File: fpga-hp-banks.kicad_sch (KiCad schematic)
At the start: 9 parts, among them U34 XCAU25P-2FFVB676I

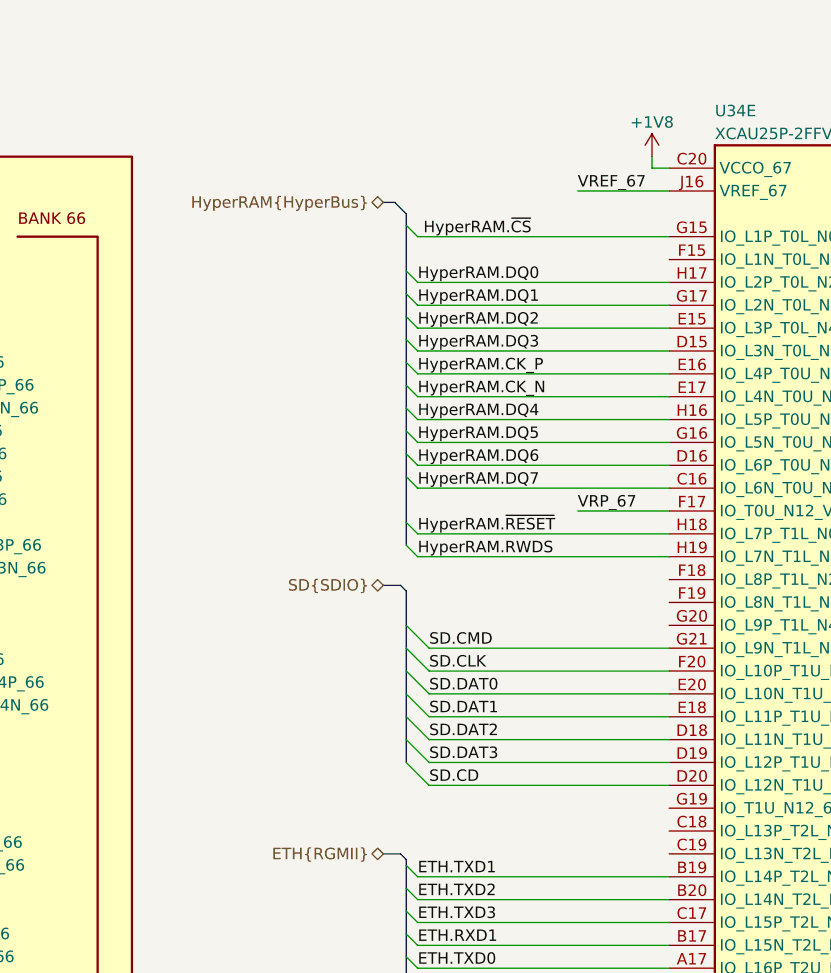
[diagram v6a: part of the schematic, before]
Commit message: [#67016] Add HyperRam layout
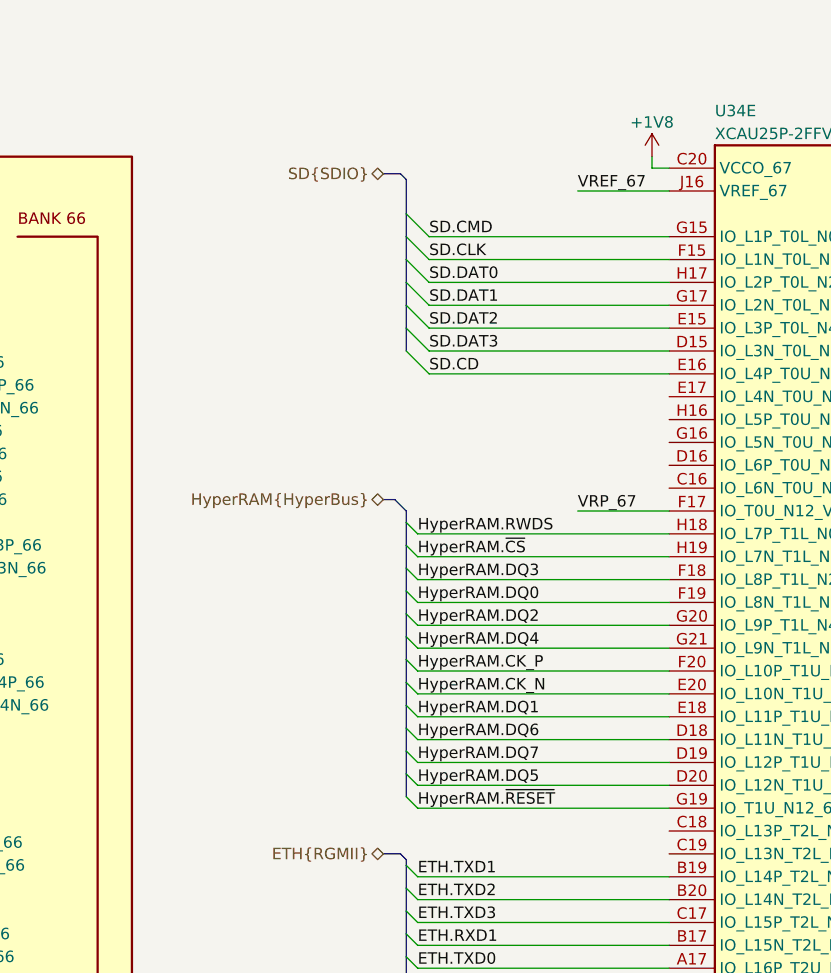
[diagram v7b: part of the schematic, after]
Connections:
- net HyperRAM.CK_N: now also U34.E20 (IO_L10N_T1U_N7_QBC_AD4N_67); no longer U34.E17 (IO_L4N_T0U_N7_DBC_AD7N_67)
- net HyperRAM.CK_P: now also U34.F20 (IO_L10P_T1U_N6_QBC_AD4P_67); no longer U34.E16 (IO_L4P_T0U_N6_DBC_AD7P_67)
- net HyperRAM.DQ0: now also U34.F19 (IO_L8N_T1L_N3_AD5N_67); no longer U34.H17 (IO_L2P_T0L_N2_67)
- net HyperRAM.DQ1: now also U34.E18 (IO_L11P_T1U_N8_GC_67); no longer U34.G17 (IO_L2N_T0L_N3_67)
- net HyperRAM.DQ2: now also U34.G20 (IO_L9P_T1L_N4_AD12P_67); no longer U34.E15 (IO_L3P_T0L_N4_AD15P_67)
- net HyperRAM.DQ3: now also U34.F18 (IO_L8P_T1L_N2_AD5P_67); no longer U34.D15 (IO_L3N_T0L_N5_AD15N_67)
- net HyperRAM.DQ4: now also U34.G21 (IO_L9N_T1L_N5_AD12N_67); no longer U34.H16 (IO_L5P_T0U_N8_AD14P_67)
- net HyperRAM.DQ5: now also U34.D20 (IO_L12N_T1U_N11_GC_67); no longer U34.G16 (IO_L5N_T0U_N9_AD14N_67)
- net HyperRAM.DQ6: now also U34.D18 (IO_L11N_T1U_N9_GC_67); no longer U34.D16 (IO_L6P_T0U_N10_AD6P_67)
- net HyperRAM.DQ7: now also U34.D19 (IO_L12P_T1U_N10_GC_67); no longer U34.C16 (IO_L6N_T0U_N11_AD6N_67)
- net HyperRAM.RWDS: now also U34.H18 (IO_L7P_T1L_N0_QBC_AD13P_67); no longer U34.H19 (IO_L7N_T1L_N1_QBC_AD13N_67)
- net HyperRAM.~{CS}: now also U34.H19 (IO_L7N_T1L_N1_QBC_AD13N_67); no longer U34.G15 (IO_L1P_T0L_N0_DBC_67)
- net HyperRAM.~{RESET}: now also U34.G19 (IO_T1U_N12_67); no longer U34.H18 (IO_L7P_T1L_N0_QBC_AD13P_67)
- net SD.CD: now also U34.E16 (IO_L4P_T0U_N6_DBC_AD7P_67); no longer U34.D20 (IO_L12N_T1U_N11_GC_67)
- net SD.CLK: now also U34.F15 (IO_L1N_T0L_N1_DBC_67); no longer U34.F20 (IO_L10P_T1U_N6_QBC_AD4P_67)
- net SD.CMD: now also U34.G15 (IO_L1P_T0L_N0_DBC_67); no longer U34.G21 (IO_L9N_T1L_N5_AD12N_67)
- net SD.DAT0: now also U34.H17 (IO_L2P_T0L_N2_67); no longer U34.E20 (IO_L10N_T1U_N7_QBC_AD4N_67)
- net SD.DAT1: now also U34.G17 (IO_L2N_T0L_N3_67); no longer U34.E18 (IO_L11P_T1U_N8_GC_67)
- net SD.DAT2: now also U34.E15 (IO_L3P_T0L_N4_AD15P_67); no longer U34.D18 (IO_L11N_T1U_N9_GC_67)
- net SD.DAT3: now also U34.D15 (IO_L3N_T0L_N5_AD15N_67); no longer U34.D19 (IO_L12P_T1U_N10_GC_67)

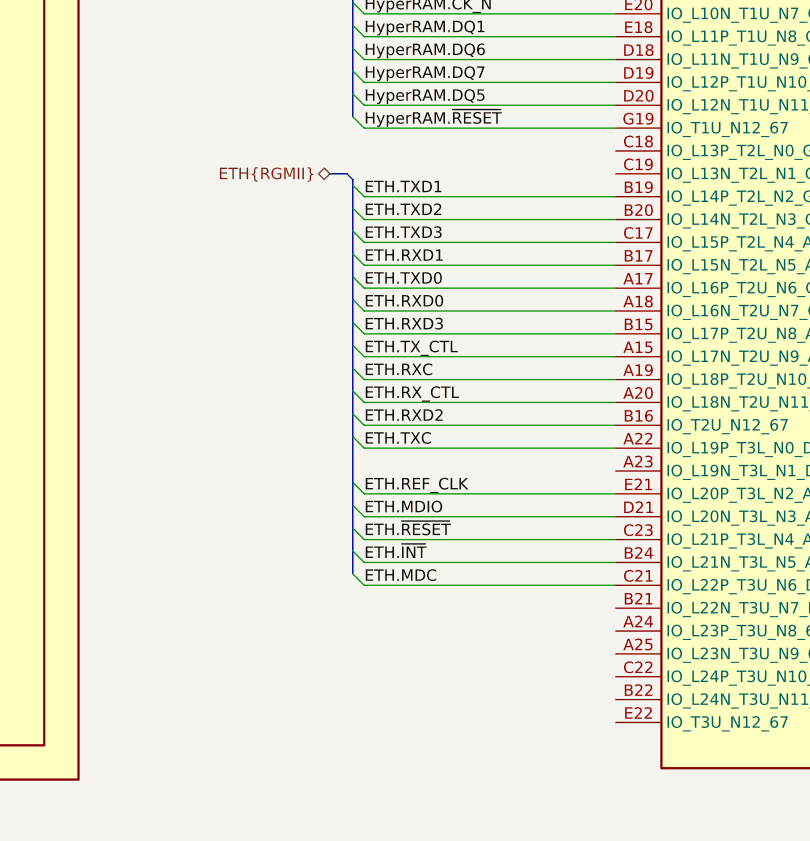
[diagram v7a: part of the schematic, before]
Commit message: [#67016] Remap RGMII interface
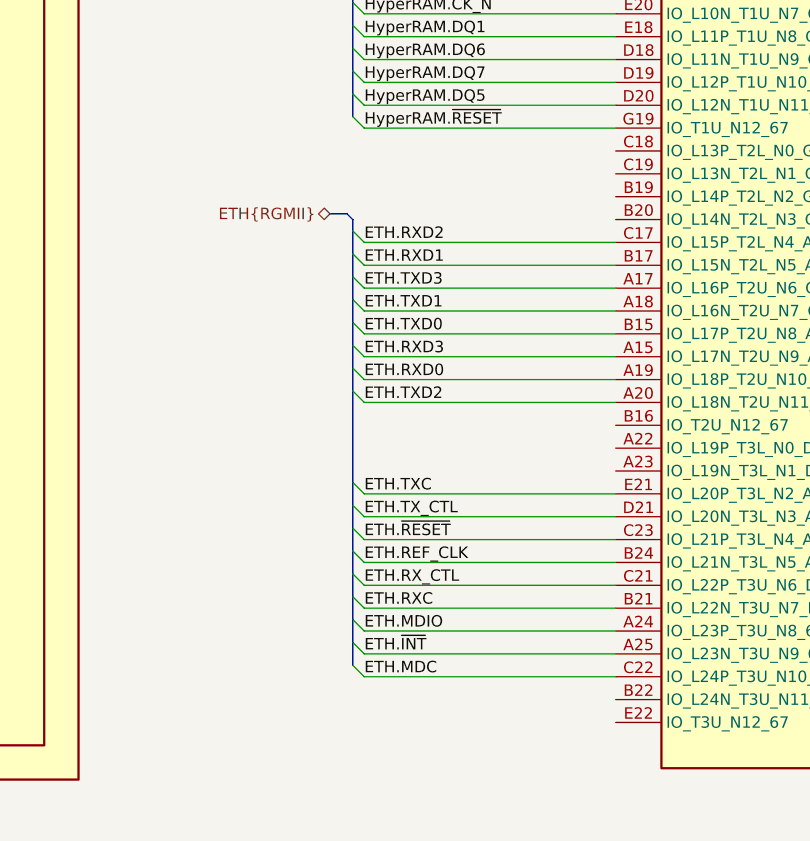
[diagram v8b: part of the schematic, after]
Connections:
- net ETH.MDC: now also U34.C22 (IO_L24P_T3U_N10_67); no longer U34.C21 (IO_L22P_T3U_N6_DBC_AD0P_67)
- net ETH.MDIO: now also U34.A24 (IO_L23P_T3U_N8_67); no longer U34.D21 (IO_L20N_T3L_N3_AD1N_67)
- net ETH.REF_CLK: now also U34.B24 (IO_L21N_T3L_N5_AD8N_67); no longer U34.E21 (IO_L20P_T3L_N2_AD1P_67)
- net ETH.RXC: now also U34.B21 (IO_L22N_T3U_N7_DBC_AD0N_67); no longer U34.A19 (IO_L18P_T2U_N10_AD2P_67)
- net ETH.RXD0: now also U34.A19 (IO_L18P_T2U_N10_AD2P_67); no longer U34.A18 (IO_L16N_T2U_N7_QBC_AD3N_67)
- net ETH.RXD2: now also U34.C17 (IO_L15P_T2L_N4_AD11P_67); no longer U34.B16 (IO_T2U_N12_67)
- net ETH.RXD3: now also U34.A15 (IO_L17N_T2U_N9_AD10N_67); no longer U34.B15 (IO_L17P_T2U_N8_AD10P_67)
- net ETH.RX_CTL: now also U34.C21 (IO_L22P_T3U_N6_DBC_AD0P_67); no longer U34.A20 (IO_L18N_T2U_N11_AD2N_67)
- net ETH.TXC: now also U34.E21 (IO_L20P_T3L_N2_AD1P_67); no longer U34.A22 (IO_L19P_T3L_N0_DBC_AD9P_67)
- net ETH.TXD0: now also U34.B15 (IO_L17P_T2U_N8_AD10P_67); no longer U34.A17 (IO_L16P_T2U_N6_QBC_AD3P_67)
- net ETH.TXD1: now also U34.A18 (IO_L16N_T2U_N7_QBC_AD3N_67); no longer U34.B19 (IO_L14P_T2L_N2_GC_67)
- net ETH.TXD2: now also U34.A20 (IO_L18N_T2U_N11_AD2N_67); no longer U34.B20 (IO_L14N_T2L_N3_GC_67)
- net ETH.TXD3: now also U34.A17 (IO_L16P_T2U_N6_QBC_AD3P_67); no longer U34.C17 (IO_L15P_T2L_N4_AD11P_67)
- net ETH.TX_CTL: now also U34.D21 (IO_L20N_T3L_N3_AD1N_67); no longer U34.A15 (IO_L17N_T2U_N9_AD10N_67)
- net ETH.~{INT}: now also U34.A25 (IO_L23N_T3U_N9_67); no longer U34.B24 (IO_L21N_T3L_N5_AD8N_67)
